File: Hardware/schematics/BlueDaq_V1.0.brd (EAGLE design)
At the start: 67 x 72 mm, 75 parts, among them IC1 MEGA8-AI, Q1 MMBT2222, Q2 MMBT2222, Q3 MMBT2222, Q4 MMBT2222, U1 MCP73831, U2 TPS61200, U3 BME280, U4 MIC5225-3.3, U5 MIC5219 5V, X1 USB-MICROB, X2 3.5mm, X4 3.5mm, Y1 16 mhz

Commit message: Minor fixes
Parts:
- moved +9V 0.10 mm to (19.5, 50.5)
- moved -9V 0.10 mm to (26.5, 50.5)
- moved C1 0.10 mm to (63.5, 51.9)
- moved C10 0.10 mm to (51.5, 60.5)
- moved C11 0.10 mm to (29.5, 38.0)
- moved C12 0.10 mm to (28.5, 58.5)
- moved C13 0.10 mm to (23.0, 50.5)
- moved C14 0.10 mm to (18.0, 27.5)
- moved C15 0.10 mm to (19.5, 56.0)
- moved C2 0.10 mm to (63.5, 35.0)
- moved C4 0.10 mm to (42.5, 57.7)
- moved C5 0.10 mm to (31.5, 56.5)
- moved C6 0.10 mm to (32.0, 62.5)
- moved C9 0.10 mm to (60.0, 62.5)
- moved D1 0.10 mm to (30.5, 19.5)
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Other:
- board size 67 x 72 mm -> 67.1 x 72 mm

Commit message: naming
special for andy
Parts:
- moved +9V 0.10 mm to (19.6, 50.5)
- moved -9V 0.10 mm to (26.6, 50.5)
- moved C1 0.10 mm to (63.6, 51.9)
- moved C10 0.10 mm to (51.6, 60.5)
- moved C11 0.10 mm to (29.6, 38.0)
- moved C12 0.10 mm to (28.6, 58.5)
- moved C13 0.10 mm to (23.1, 50.5)
- moved C14 0.10 mm to (18.1, 27.5)
- moved C15 0.10 mm to (19.6, 56.0)
- moved C2 0.10 mm to (63.6, 35.0)
- moved C4 0.10 mm to (42.6, 57.7)
- moved C5 0.10 mm to (31.6, 56.5)
- moved C6 0.10 mm to (32.1, 62.5)
- moved C9 0.10 mm to (60.1, 62.5)
- moved D1 0.10 mm to (30.6, 19.5)
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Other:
- board size 67.1 x 72 mm -> 67 x 72 mm

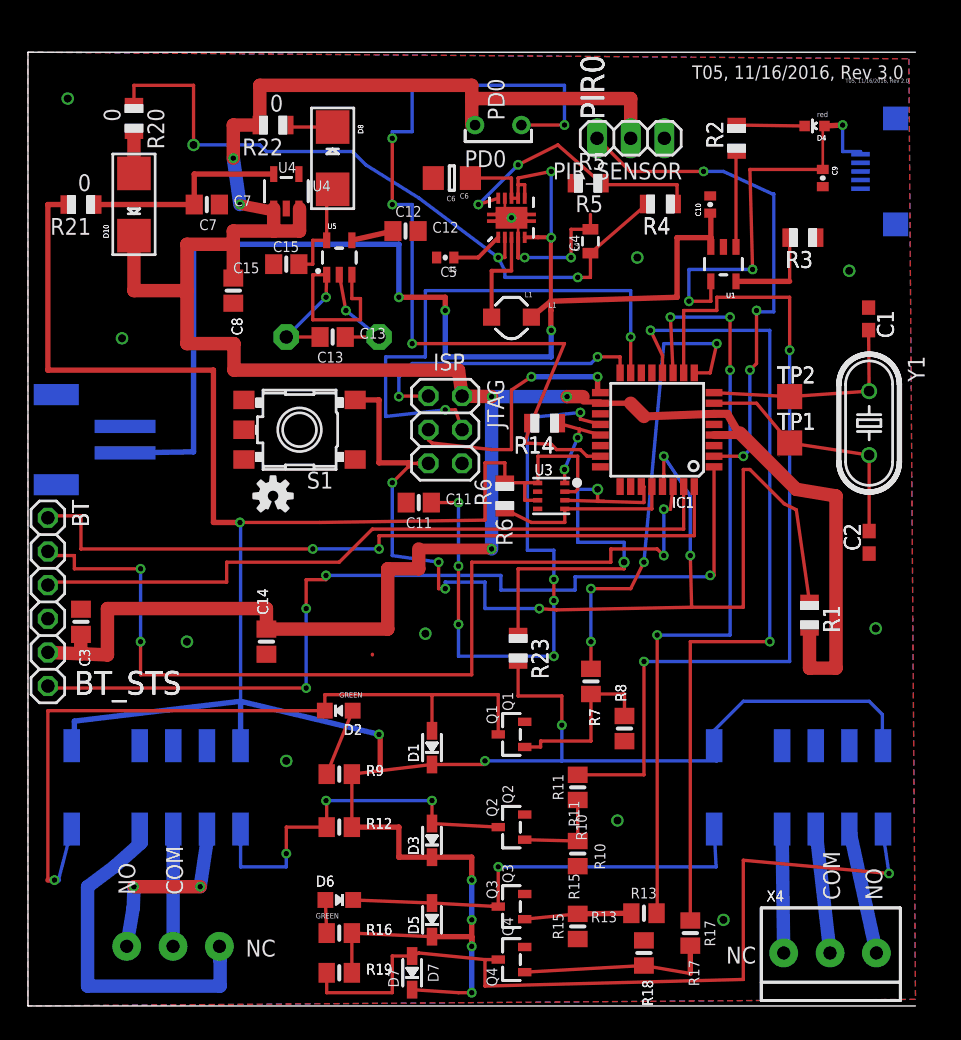
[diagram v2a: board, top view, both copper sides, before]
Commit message: Corrected posts to bottom layer
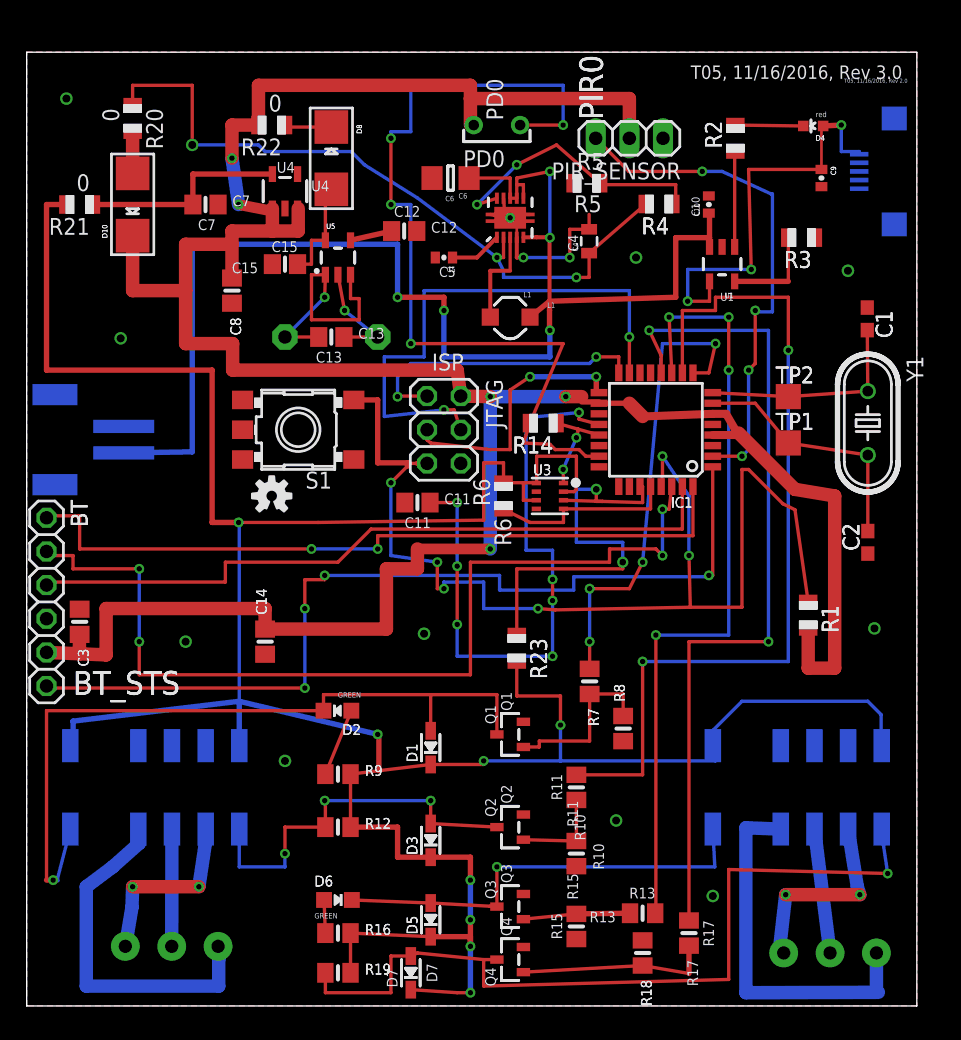
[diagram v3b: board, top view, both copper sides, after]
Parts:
- moved +9V 0.10 mm to (19.5, 50.5)
- moved -9V 0.10 mm to (26.5, 50.5)
- moved C1 0.10 mm to (63.5, 51.9)
- moved C10 0.10 mm to (51.5, 60.5)
- moved C11 0.10 mm to (29.5, 38.0)
- moved C12 0.10 mm to (28.5, 58.5)
- moved C13 0.10 mm to (23.0, 50.5)
- moved C14 0.10 mm to (18.0, 27.5)
- moved C15 0.10 mm to (19.5, 56.0)
- moved C2 0.10 mm to (63.5, 35.0)
- moved C4 0.10 mm to (42.5, 57.7)
- moved C5 0.10 mm to (31.5, 56.5)
- moved C6 0.10 mm to (32.0, 62.5)
- moved C9 0.10 mm to (60.0, 62.5)
- moved D1 0.10 mm to (30.5, 19.5)
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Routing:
- net N$10: track 9.35 -> 28.2 mm
- net NO2: track 9.57 -> 15.4 mm, vias 0 -> 2
- net GND: track 20.7 -> 24.1 mm, vias 5 -> 15
- net N$12: track 62.3 -> 61.5 mm
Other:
- board size 67 x 72 mm -> 67.2 x 72 mm
- board text removed: "X4"

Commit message: oh no fix
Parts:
- C1, C2: device rcl:C0603 -> rcl:C0805
- C10, C5, C9: device SparkFun:0402-CAP -> SparkFun:0805
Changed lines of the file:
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@@
 <element name="+9V" library="adafruit" package="1X01" value="" x="19.5" y="50.5" rot="MR0"/>
 <element name="-9V" library="adafruit" package="1X01" value="" x="26.5" y="50.5" rot="MR0"/>
-<element name="C1" library="rcl" package="C0603" value="22p" x="63.46" y="51.87" rot="R270"/>
-<element name="C10" library="SparkFun" package="0402-CAP" value="4.7uF" x="51.5" y="60.5" rot="R90"/>
+<element name="C1" library="rcl" package="C0805" value="22p" x="63.46" y="51.87" rot="R270"/>
+<element name="C10" library="SparkFun" package="0805" value="4.7uF" x="51.5" y="60.5" rot="R90"/>
 <element name="C12" library="microbuilder" package="0805-NO@1" value=".1uF" x="28.5" y="58.5"/>
-<element name="C2" library="rcl" package="C0603" value="22p" x="63.5" y="35" rot="R90"/>
+<element name="C2" library="rcl" package="C0805" value="22p" x="63.5" y="35" rot="R90"/>
 <element name="C4" library="CH_passive" package="0805" value="22uF" x="42.46" y="57.73" rot="R90"/>
-<element name="C5" library="SparkFun" package="0402-CAP" value="0.1uF" x="31.5" y="56.5" rot="R180"/>
+<element name="C5" library="SparkFun" package="0805" value="0.1uF" x="31.5" y="56.5" rot="R180"/>
 <element name="C6" library="CH_passive" package="1206" value="10uF" x="32" y="62.5" rot="R180"/>
 <element name="C7" library="microbuilder" package="0805-NO@1" value="10uF" x="13.5" y="60.5"/>
 <element name="C8" library="microbuilder" package="0805-NO@1" value="10uF" x="15.5" y="54" rot="R270"/>
-<element name="C9" library="SparkFun" package="0402-CAP" value="4.7uF" x="60" y="62.5" rot="R270"/>
+<element name="C9" library="SparkFun" package="0805" value="4.7uF" x="60" y="62.5" rot="R270"/>
 <element name="D1" library="microbuilder" package="SOD-323" value="1N4148" x="30.5" y="19.5" rot="R90"/>
 <element name="D2" library="microbuilder" package="CHIPLED_0805_NOOUTLINE" value="GREEN" x="23.46" y="22.29" rot="R90"/>
@@
 <contactref element="TP1" pad="TP"/>
 <wire x1="57.5" y1="42.5" x2="63.5" y2="41.587" width="0.254" layer="1"/>
-<wire x1="63.5" y1="35.85" x2="63.5" y2="41.587" width="0.254" layer="1"/>
+<wire x1="63.5" y1="35.95" x2="63.5" y2="41.587" width="0.254" layer="1"/>
 <wire x1="57.5" y1="42.5" x2="55" y2="45.5" width="0.254" layer="1"/>
 <wire x1="55" y1="45.5" x2="51.7926" y2="45.5" width="0.254" layer="1"/>
@@
 <contactref element="IC1" pad="8"/>
 <contactref element="TP2" pad="TP"/>
-<wire x1="63.46" y1="51.02" x2="63.5" y2="46.413" width="0.254" layer="1"/>
+<wire x1="63.46" y1="50.92" x2="63.5" y2="46.413" width="0.254" layer="1"/>
 <wire x1="63.5" y1="46.413" x2="57.5" y2="46" width="0.254" layer="1"/>
 <wire x1="57.5" y1="46" x2="51.7926" y2="46.3" width="0.254" layer="1"/>
@@
 <wire x1="51.55" y1="57.3001" x2="51.55" y2="58" width="0.4064" layer="1"/>
 <wire x1="51.55" y1="58" x2="51.55" y2="59.85" width="0.4064" layer="1"/>
-<wire x1="51.55" y1="59.85" x2="51.5" y2="59.85" width="0.254" layer="1"/>
+<wire x1="51.55" y1="59.85" x2="51.5" y2="59.6" width="0.254" layer="1"/>
 <wire x1="7.33" y1="41.75" x2="12.5" y2="41.83" width="0.4064" layer="16"/>
 <wire x1="12.5" y1="41.83" x2="12.5" y2="57.5" width="0.4064" layer="16"/>
@@
 <contactref element="C5" pad="1"/>
 <contactref element="U2" pad="1"/>
-<wire x1="32.15" y1="56.5" x2="34" y2="56.5" width="0.3048" layer="1"/>
+<wire x1="32.4" y1="56.5" x2="34" y2="56.5" width="0.3048" layer="1"/>
 <wire x1="34" y1="56.5" x2="35.5" y2="58.025" width="0.3048" layer="1"/>
 </signal>
@@
 <via x="61.5" y="66.5" extent="1-16" drill="0.4"/>
 <wire x1="60" y1="66.43" x2="60.13" y2="66.43" width="0.4064" layer="1"/>
-<wire x1="60" y1="66.43" x2="60" y2="63.15" width="0.2032" layer="1"/>
+<wire x1="60" y1="66.43" x2="60" y2="63.4" width="0.2032" layer="1"/>
 <wire x1="61.5" y1="66.5" x2="61.5" y2="64.5" width="0.254" layer="16"/>
 <wire x1="61.5" y1="64.5" x2="62.85" y2="64.5" width="0.254" layer="16"/>
 <wire x1="62.85" y1="64.5" x2="62.85" y2="64.3" width="0.254" layer="16"/>
 <contactref element="U1" pad="4"/>
-<wire x1="60" y1="63.15" x2="54.5" y2="63.15" width="0.254" layer="1"/>
+<wire x1="60" y1="63.4" x2="54.5" y2="63.15" width="0.254" layer="1"/>
 <wire x1="54.5" y1="63.15" x2="54.7" y2="55.6" width="0.254" layer="1"/>
 <via x="54.7" y="55.6" extent="1-16" drill="0.4"/>

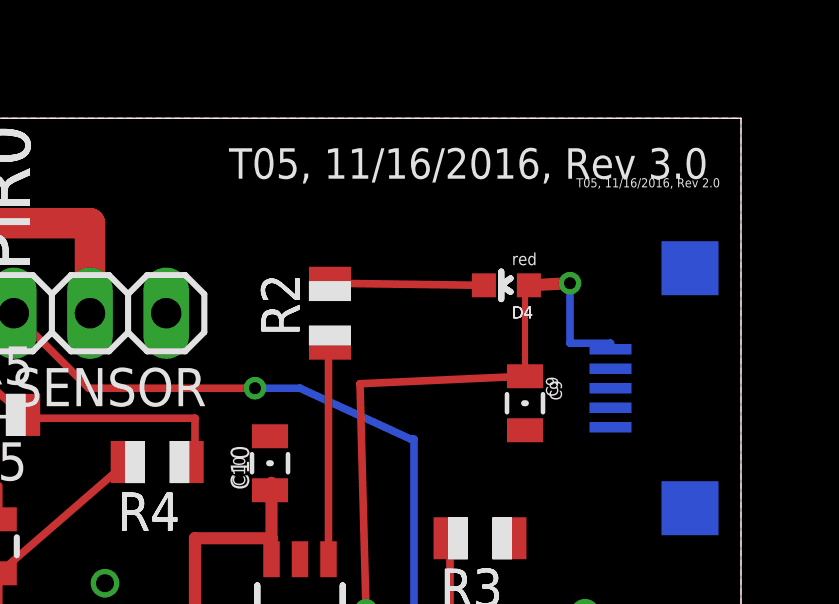
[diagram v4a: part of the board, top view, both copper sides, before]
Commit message: fixed comps being too dang small
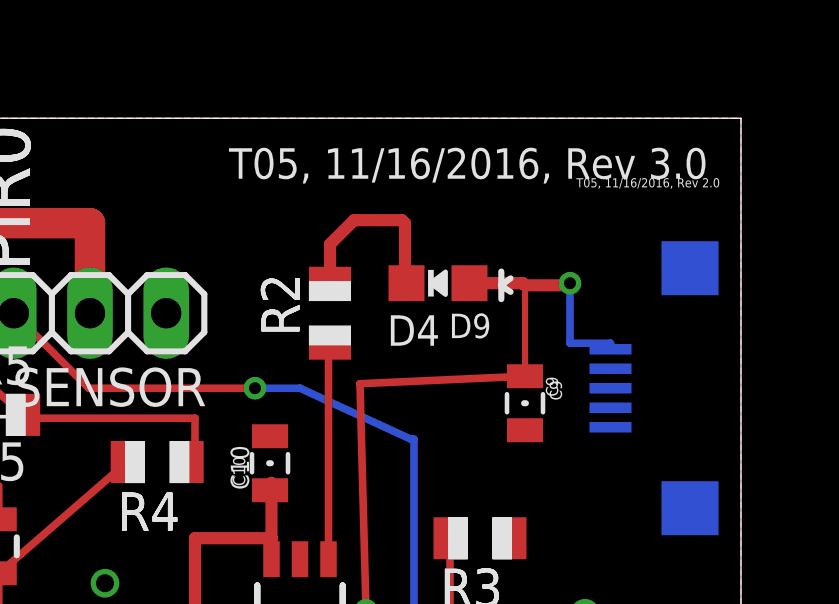
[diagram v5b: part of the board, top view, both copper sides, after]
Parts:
- removed D4: red, SparkFun:LED-0603
- added D9: GREEN, microbuilder:CHIPLED_0805_NOOUTLINE
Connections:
- net N$23: now also D9.A; no longer D4.A
- net N$4: now also D9.C; no longer D4.C
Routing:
- net N$23: track 31.5 -> 33.4 mm
- net N$4: track 5.13 -> 6.19 mm
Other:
- board text removed: "red"
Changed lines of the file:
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@@
 <wire x1="59.209990625" y1="66.429990625" x2="59.52" y2="66.6638" width="0.2032" layer="121"/>
 <wire x1="59.225409375" y1="66.404590625" x2="59.52" y2="66.211603125" width="0.2032" layer="121"/>
-<text x="60.26899375" y="65.731490625" size="0.4064" layer="121" ratio="31" rot="R180">D4</text>
-<text x="60.39599375" y="67.509490625" size="0.4064" layer="121" ratio="31" rot="R180">red</text>
+<text x="57.16899375" y="65.431490625" size="1.016" layer="121" ratio="31" rot="R180">D4</text>
 <wire x1="29.79999375" y1="5.4999875" x2="29.79999375" y2="7.500009375" width="0.2032" layer="121"/>
 <wire x1="31.199990625" y1="7.500009375" x2="31.199990625" y2="5.4999875" width="0.2032" layer="121"/>
@@
 <element name="D2" library="microbuilder" package="CHIPLED_0805_NOOUTLINE" value="GREEN" x="23.46" y="22.29" rot="R90"/>
 <element name="D3" library="microbuilder" package="SOD-323" value="1N4148" x="30.5" y="12.5" rot="R90"/>
-<element name="D4" library="SparkFun" package="LED-0603" value="red" x="59.38" y="66.43" rot="R90"/>
 <element name="D5" library="microbuilder" package="SOD-323" value="1N4148" x="30.5" y="6.5" rot="R90"/>
 <element name="D6" library="microbuilder" package="CHIPLED_0805_NOOUTLINE" value="GREEN" x="23.5" y="8" rot="R270"/>
@@
 <element name="C13" library="microbuilder" package="0805-NO@1" value="10uF" x="23" y="50.5"/>
 <element name="C15" library="microbuilder" package="0805-NO@1" value="10uF" x="19.5" y="56" rot="R180"/>
+<element name="D9" library="microbuilder" package="CHIPLED_0805_NOOUTLINE" value="GREEN" x="57.1" y="66.5" rot="R90"/>
 </elements>
 <signals>
@@
 </signal>
 <signal name="N$4">
-<contactref element="D4" pad="C"/>
 <contactref element="R2" pad="2"/>
-<wire x1="58.63" y1="66.43" x2="53.5" y2="66.5" width="0.254" layer="1"/>
+<contactref element="D9" pad="C"/>
+<wire x1="53.5" y1="66.5" x2="53.5" y2="67.8" width="0.4064" layer="1"/>
+<wire x1="53.5" y1="67.8" x2="54.3" y2="68.6" width="0.4064" layer="1"/>
+<wire x1="54.3" y1="68.6" x2="55.9" y2="68.6" width="0.4064" layer="1"/>
+<wire x1="55.9" y1="68.6" x2="56" y2="68.5" width="0.4064" layer="1"/>
+<wire x1="56" y1="68.5" x2="56" y2="66.55" width="0.4064" layer="1"/>
+<wire x1="56" y1="66.55" x2="56.05" y2="66.5" width="0.4064" layer="1"/>
 </signal>
 <signal name="N$6">
@@
 <signal name="N$23">
 <contactref element="C9" pad="1"/>
-<contactref element="D4" pad="A"/>
 <contactref element="X1" pad="VBUS"/>
-<wire x1="60.13" y1="66.43" x2="61.5" y2="66.5" width="0.4064" layer="1"/>
 <via x="61.5" y="66.5" extent="1-16" drill="0.4"/>
-<wire x1="60" y1="66.43" x2="60.13" y2="66.43" width="0.4064" layer="1"/>
 <wire x1="60" y1="66.43" x2="60" y2="63.4" width="0.2032" layer="1"/>
 <wire x1="61.5" y1="66.5" x2="61.5" y2="64.5" width="0.254" layer="16"/>
@@
 <wire x1="49.9" y1="53.2" x2="51.55" y2="53.2" width="0.254" layer="1"/>
 <wire x1="51.55" y1="53.2" x2="51.55" y2="54.6999" width="0.254" layer="1"/>
+<contactref element="D9" pad="A"/>
+<wire x1="58.15" y1="66.5" x2="59.93" y2="66.5" width="0.4064" layer="1"/>
+<wire x1="59.93" y1="66.5" x2="60" y2="66.43" width="0.4064" layer="1"/>
+<wire x1="60" y1="66.43" x2="61.43" y2="66.43" width="0.4064" layer="1"/>
+<wire x1="61.43" y1="66.43" x2="61.5" y2="66.5" width="0.4064" layer="1"/>
 </signal>
 <signal name="N$5">
